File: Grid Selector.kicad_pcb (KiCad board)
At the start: 2 copper layers, 92 parts, among them SW1 MX_SW_HS, SW10 MX_SW_HS, SW11 MX_SW_HS, SW12 MX_SW_HS, SW13 MX_SW_HS, SW14 MX_SW_HS, SW15 MX_SW_HS, SW16 MX_SW_HS, SW17 MX_SW_HS, SW18 MX_SW_HS, SW19 MX_SW_HS, SW2 MX_SW_HS, SW20 MX_SW_HS, SW21 MX_SW_HS, SW22 MX_SW_HS, SW23 MX_SW_HS, SW24 MX_SW_HS, SW25 MX_SW_HS, SW26 MX_SW_HS, SW27 MX_SW_HS, SW28 MX_SW_HS, SW29 MX_SW_HS, SW3 MX_SW_HS, SW30 MX_SW_HS, SW4 MX_SW_HS, SW5 MX_SW_HS, SW6 MX_SW_HS, SW7 MX_SW_HS, SW8 MX_SW_HS, SW9 MX_SW_HS, U1 Pico

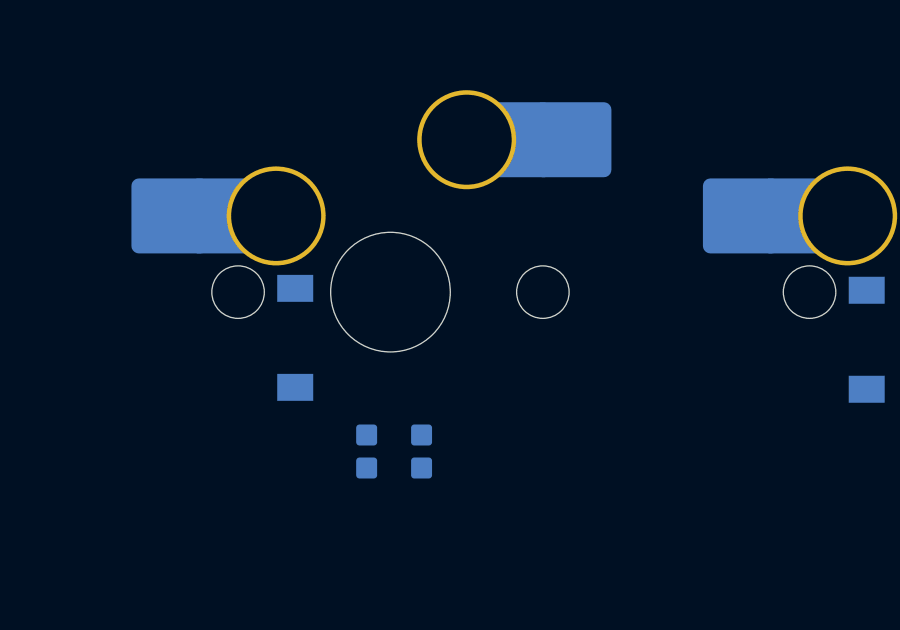
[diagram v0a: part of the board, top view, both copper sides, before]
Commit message: added current limiting resistors to led chain
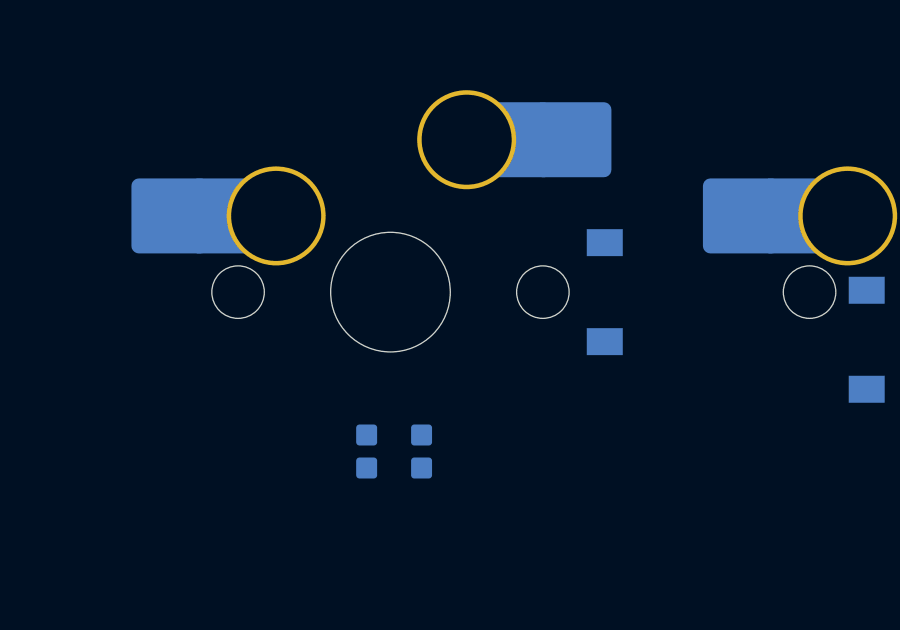
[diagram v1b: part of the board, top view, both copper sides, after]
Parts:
- moved D1 10.4 mm to (113.5, 36.5), turned to -90 degrees
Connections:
- D1 pad 1: ROW0 -> ROW2
- D10 pad 1: ROW0 -> ROW2
- D12 pad 1: ROW2 -> ROW0
- D13 pad 1: ROW0 -> ROW2
- D15 pad 1: ROW2 -> ROW0
- D16 pad 1: ROW0 -> ROW2
- D18 pad 1: ROW2 -> ROW0
- D19 pad 1: ROW0 -> ROW2
- D21 pad 1: ROW2 -> ROW0
- D22 pad 1: ROW0 -> ROW2
- D24 pad 1: ROW2 -> ROW0
- D25 pad 1: ROW0 -> ROW2
- D27 pad 1: ROW2 -> ROW0
- D3 pad 1: ROW2 -> ROW0
- D4 pad 1: ROW0 -> ROW2
- D58 pad 1: ROW0 -> ROW2
- D6 pad 1: ROW2 -> ROW0
- D60 pad 1: ROW2 -> ROW0
- D7 pad 1: ROW0 -> ROW2
- D9 pad 1: ROW2 -> ROW0
- SW1 pad 1: Net-(D1-Pad2) -> COL0
- SW1 pad 2: COL0 -> Net-(D60-Pad2)
- SW10 pad 1: Net-(D10-Pad2) -> COL3
- SW10 pad 2: COL3 -> Net-(D21-Pad2)
- SW11 pad 1: Net-(D11-Pad2) -> COL3
- SW11 pad 2: COL3 -> Net-(D20-Pad2)
- SW12 pad 1: Net-(D12-Pad2) -> COL3
- SW12 pad 2: COL3 -> Net-(D19-Pad2)
- SW13 pad 1: Net-(D13-Pad2) -> COL4
- SW13 pad 2: COL4 -> Net-(D18-Pad2)
- SW14 pad 1: Net-(D14-Pad2) -> COL4
- SW14 pad 2: COL4 -> Net-(D17-Pad2)
- SW15 pad 1: Net-(D15-Pad2) -> COL4
- SW15 pad 2: COL4 -> Net-(D16-Pad2)
- SW16 pad 1: Net-(D16-Pad2) -> COL5
- SW16 pad 2: COL5 -> Net-(D15-Pad2)
- SW17 pad 1: Net-(D17-Pad2) -> COL5
- SW17 pad 2: COL5 -> Net-(D14-Pad2)
- SW18 pad 1: Net-(D18-Pad2) -> COL5
- SW18 pad 2: COL5 -> Net-(D13-Pad2)
- SW19 pad 1: Net-(D19-Pad2) -> Net-(SW19-Pad1)
- SW19 pad 2: COL6 -> Net-(D12-Pad2)
- SW2 pad 1: Net-(D2-Pad2) -> COL0
- SW2 pad 2: COL0 -> Net-(D59-Pad2)
- SW20 pad 1: Net-(D20-Pad2) -> Net-(SW19-Pad1)
- SW20 pad 2: COL6 -> Net-(D11-Pad2)
- SW21 pad 1: Net-(D21-Pad2) -> Net-(SW19-Pad1)
- SW21 pad 2: COL6 -> Net-(D10-Pad2)
- SW22 pad 1: Net-(D22-Pad2) -> Net-(SW22-Pad1)
- SW22 pad 2: COL7 -> Net-(D9-Pad2)
- SW23 pad 1: Net-(D23-Pad2) -> Net-(SW22-Pad1)
- SW23 pad 2: COL7 -> Net-(D8-Pad2)
- SW24 pad 1: Net-(D24-Pad2) -> Net-(SW22-Pad1)
- SW24 pad 2: COL7 -> Net-(D7-Pad2)
- SW25 pad 1: Net-(D25-Pad2) -> Net-(SW25-Pad1)
- SW25 pad 2: COL8 -> Net-(D6-Pad2)
- SW26 pad 1: Net-(D26-Pad2) -> Net-(SW25-Pad1)
- SW26 pad 2: COL8 -> Net-(D5-Pad2)
- SW27 pad 1: Net-(D27-Pad2) -> Net-(SW25-Pad1)
- SW27 pad 2: COL8 -> Net-(D4-Pad2)
- SW28 pad 1: Net-(D58-Pad2) -> Net-(SW28-Pad1)
- SW28 pad 2: COL9 -> Net-(D3-Pad2)
- SW29 pad 1: Net-(D59-Pad2) -> Net-(SW28-Pad1)
- SW29 pad 2: COL9 -> Net-(D2-Pad2)
- SW3 pad 1: Net-(D3-Pad2) -> COL0
- SW3 pad 2: COL0 -> Net-(D58-Pad2)
- SW30 pad 1: Net-(D60-Pad2) -> Net-(SW28-Pad1)
- SW30 pad 2: COL9 -> Net-(D1-Pad2)
- SW4 pad 1: Net-(D4-Pad2) -> COL1
- SW4 pad 2: COL1 -> Net-(D27-Pad2)
- SW5 pad 1: Net-(D5-Pad2) -> COL1
- SW5 pad 2: COL1 -> Net-(D26-Pad2)
- SW6 pad 1: Net-(D6-Pad2) -> COL1
- SW6 pad 2: COL1 -> Net-(D25-Pad2)
- SW7 pad 1: Net-(D7-Pad2) -> COL2
- SW7 pad 2: COL2 -> Net-(D24-Pad2)
- SW8 pad 1: Net-(D8-Pad2) -> COL2
- SW8 pad 2: COL2 -> Net-(D23-Pad2)
- SW9 pad 1: Net-(D9-Pad2) -> COL2
- SW9 pad 2: COL2 -> Net-(D22-Pad2)
